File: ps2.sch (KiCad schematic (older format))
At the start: 10 parts

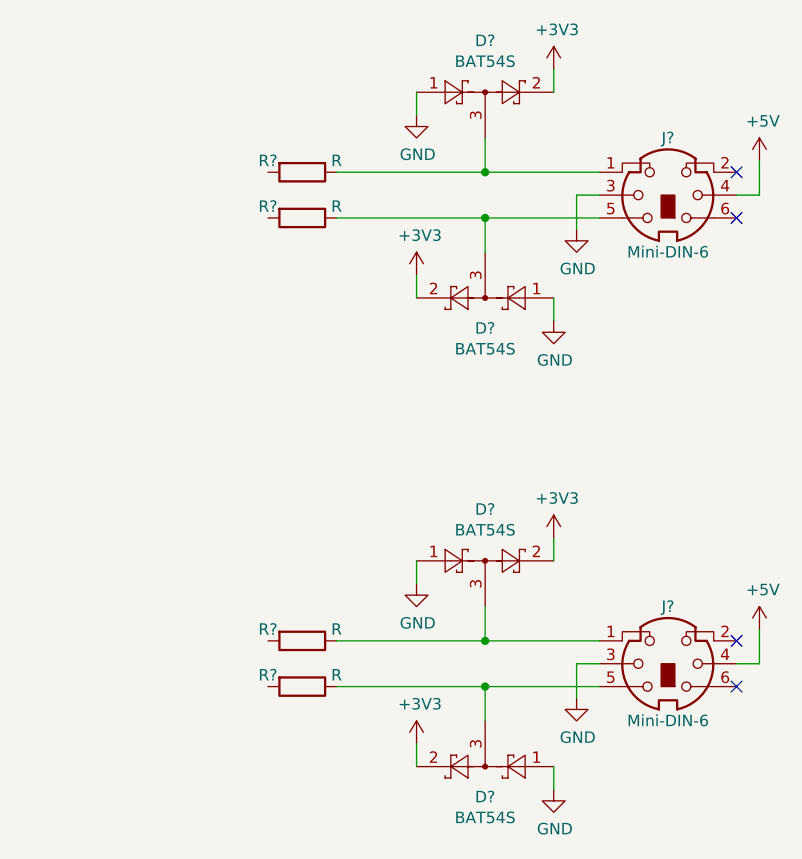
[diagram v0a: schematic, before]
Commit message: HDMI and VGA circuit added.
Signed-off-by: Kali Prasad <kprasadvnsi@protonmail.com>
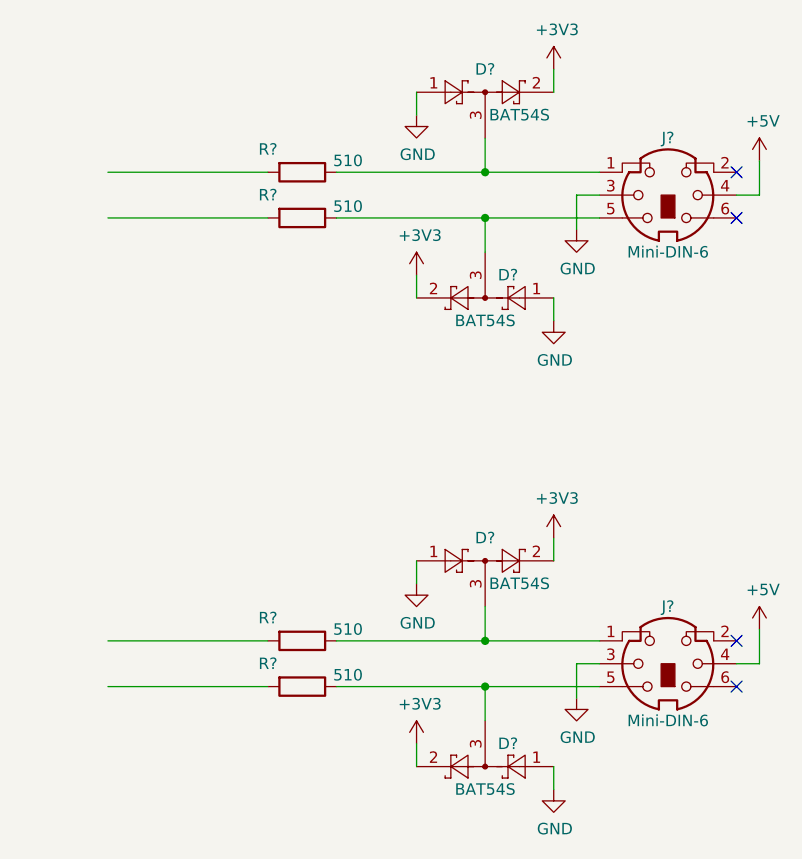
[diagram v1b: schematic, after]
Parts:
- R? (x4): value R -> 510
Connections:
- wire segments 28 -> 32
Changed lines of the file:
@@
 U 1 1 5D07F41B
 P 5150 2200
-F 0 "D?" H 5150 2425 50  0000 C CNN
-F 1 "BAT54S" H 5150 2334 50  0000 C CNN
+F 0 "D?" H 5150 2300 50  0000 C CNN
+F 1 "BAT54S" H 5300 2100 50  0000 C CNN
 F 2 "Package_TO_SOT_SMD:SOT-23" H 5225 2325 50  0001 L CNN
 F 3 "https://www.diodes.com/assets/Datasheets/ds11005.pdf" H 5030 2200 50  0001 C CNN
@@
 U 1 1 5D07FCC7
 P 5150 3100
-F 0 "D?" H 5150 3233 50  0000 C CNN
-F 1 "BAT54S" H 5150 3324 50  0000 C CNN
+F 0 "D?" H 5050 3000 50  0000 C CNN
+F 1 "BAT54S" H 5150 3200 50  0000 C CNN
 F 2 "Package_TO_SOT_SMD:SOT-23" H 5225 3225 50  0001 L CNN
 F 3 "https://www.diodes.com/assets/Datasheets/ds11005.pdf" H 5030 3100 50  0001 C CNN
@@
 U 1 1 5D080306
 P 4350 2550
-F 0 "R?" V 4300 2400 50  0000 C CNN
-F 1 "R" V 4300 2700 50  0000 C CNN
+F 0 "R?" V 4250 2400 50  0000 C CNN
+F 1 "510" V 4300 2750 50  0000 C CNN
 F 2 "" V 4280 2550 50  0001 C CNN
 F 3 "~" H 4350 2550 50  0001 C CNN
@@
 U 1 1 5D080849
 P 4350 2750
-F 0 "R?" V 4300 2600 50  0000 C CNN
-F 1 "R" V 4300 2900 50  0000 C CNN
+F 0 "R?" V 4250 2600 50  0000 C CNN
+F 1 "510" V 4300 2950 50  0000 C CNN
 F 2 "" V 4280 2750 50  0001 C CNN
 F 3 "~" H 4350 2750 50  0001 C CNN
@@
 U 1 1 5D0BA90B
 P 5150 4250
-F 0 "D?" H 5150 4475 50  0000 C CNN
-F 1 "BAT54S" H 5150 4384 50  0000 C CNN
+F 0 "D?" H 5150 4350 50  0000 C CNN
+F 1 "BAT54S" H 5300 4150 50  0000 C CNN
 F 2 "Package_TO_SOT_SMD:SOT-23" H 5225 4375 50  0001 L CNN
 F 3 "https://www.diodes.com/assets/Datasheets/ds11005.pdf" H 5030 4250 50  0001 C CNN
@@
 U 1 1 5D0BA915
 P 5150 5150
-F 0 "D?" H 5150 5283 50  0000 C CNN
-F 1 "BAT54S" H 5150 5374 50  0000 C CNN
+F 0 "D?" H 5050 5050 50  0000 C CNN
+F 1 "BAT54S" H 5150 5250 50  0000 C CNN
 F 2 "Package_TO_SOT_SMD:SOT-23" H 5225 5275 50  0001 L CNN
 F 3 "https://www.diodes.com/assets/Datasheets/ds11005.pdf" H 5030 5150 50  0001 C CNN
@@
 U 1 1 5D0BA91F
 P 4350 4600
-F 0 "R?" V 4300 4450 50  0000 C CNN
-F 1 "R" V 4300 4750 50  0000 C CNN
+F 0 "R?" V 4250 4450 50  0000 C CNN
+F 1 "510" V 4300 4800 50  0000 C CNN
 F 2 "" V 4280 4600 50  0001 C CNN
 F 3 "~" H 4350 4600 50  0001 C CNN
@@
 U 1 1 5D0BA929
 P 4350 4800
-F 0 "R?" V 4300 4650 50  0000 C CNN
-F 1 "R" V 4300 4950 50  0000 C CNN
+F 0 "R?" V 4250 4650 50  0000 C CNN
+F 1 "510" V 4300 5000 50  0000 C CNN
 F 2 "" V 4280 4800 50  0001 C CNN
 F 3 "~" H 4350 4800 50  0001 C CNN
@@
 Wire Wire Line
 	6350 4550 6350 4700
+Wire Wire Line
+	4200 2550 3500 2550
+Wire Wire Line
+	4200 2750 3500 2750
+Wire Wire Line
+	4200 4600 3500 4600
+Wire Wire Line
+	4200 4800 3500 4800
 $EndSCHEMATC

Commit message: SOM added.
Signed-off-by: Kali Prasad <kprasadvnsi@protonmail.com>
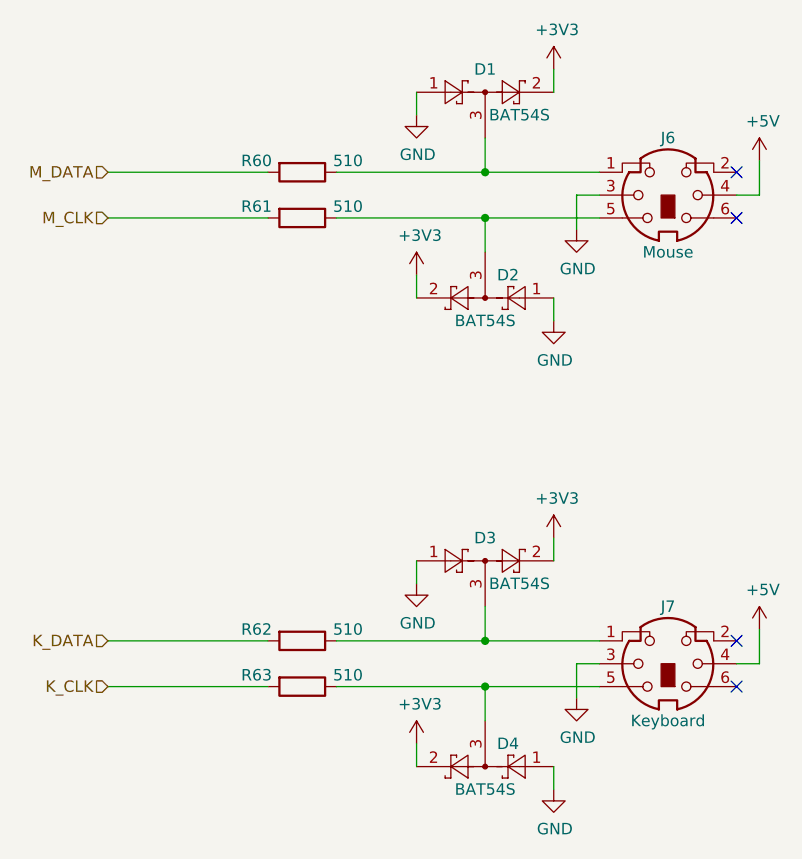
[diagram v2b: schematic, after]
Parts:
- J6: renamed from J?; value Mini-DIN-6 -> Mouse; footprint (none) -> lt_eval_board:Mini_din6
- J7: renamed from J?; value Mini-DIN-6 -> Keyboard; footprint (none) -> lt_eval_board:Mini_din6
- R60, R61, R62, R63: renamed from R?; footprint (none) -> Resistor_SMD:R_0805_2012Metric_Pad1.15x1.40mm_HandSolder
- gave numbers to parts that had none: 4
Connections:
- net labels added: K_CLK, K_DATA, M_CLK, M_DATA
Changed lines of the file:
@@
 $Descr A4 11693 8268
 encoding utf-8
-Sheet 7 7
+Sheet 4 8
 Title "LT_Eval_board"
 Date "2019-06-16"
@@
 $EndDescr
 $Comp
-L Diode:BAT54S D?
+L Diode:BAT54S D1
 U 1 1 5D07F41B
 P 5150 2200
-F 0 "D?" H 5150 2300 50  0000 C CNN
+F 0 "D1" H 5150 2300 50  0000 C CNN
 F 1 "BAT54S" H 5300 2100 50  0000 C CNN
 F 2 "Package_TO_SOT_SMD:SOT-23" H 5225 2325 50  0001 L CNN
@@
 $EndComp
 $Comp
-L Diode:BAT54S D?
+L Diode:BAT54S D2
 U 1 1 5D07FCC7
 P 5150 3100
-F 0 "D?" H 5050 3000 50  0000 C CNN
+F 0 "D2" H 5050 3000 50  0000 C CNN
 F 1 "BAT54S" H 5150 3200 50  0000 C CNN
 F 2 "Package_TO_SOT_SMD:SOT-23" H 5225 3225 50  0001 L CNN
@@
 $EndComp
 $Comp
-L Device:R R?
+L Device:R R60
 U 1 1 5D080306
 P 4350 2550
-F 0 "R?" V 4250 2400 50  0000 C CNN
+F 0 "R60" V 4300 2350 50  0000 C CNN
 F 1 "510" V 4300 2750 50  0000 C CNN
-F 2 "" V 4280 2550 50  0001 C CNN
+F 2 "Resistor_SMD:R_0805_2012Metric_Pad1.15x1.40mm_HandSolder" V 4280 2550 50  0001 C CNN
 F 3 "~" H 4350 2550 50  0001 C CNN
 	1    4350 2550
@@
 $EndComp
 $Comp
-L Device:R R?
+L Device:R R61
 U 1 1 5D080849
 P 4350 2750
-F 0 "R?" V 4250 2600 50  0000 C CNN
+F 0 "R61" V 4300 2550 50  0000 C CNN
 F 1 "510" V 4300 2950 50  0000 C CNN
-F 2 "" V 4280 2750 50  0001 C CNN
+F 2 "Resistor_SMD:R_0805_2012Metric_Pad1.15x1.40mm_HandSolder" V 4280 2750 50  0001 C CNN
 F 3 "~" H 4350 2750 50  0001 C CNN
 	1    4350 2750
@@
 $EndComp
 $Comp
-L Connector:Mini-DIN-6 J?
+L Connector:Mini-DIN-6 J6
 U 1 1 5D07D04B
 P 5950 2650
-F 0 "J?" H 5950 2400 50  0000 C CNN
-F 1 "Mini-DIN-6" H 5950 2900 50  0000 C CNN
-F 2 "" H 5950 2650 50  0001 C CNN
+F 0 "J6" H 5950 2400 50  0000 C CNN
+F 1 "Mouse" H 5950 2900 50  0000 C CNN
+F 2 "lt_eval_board:Mini_din6" H 5950 2650 50  0001 C CNN
 F 3 "http://service.powerdynamics.com/ec/Catalog17/Section%2011.pdf" H 5950 2650 50  0001 C CNN
 	1    5950 2650
@@
 	5150 2550 5650 2550
 $Comp
-L power:GND #PWR?
+L power:GND #PWR028
 U 1 1 5D094AF6
 P 4850 2300
-F 0 "#PWR?" H 4850 2050 50  0001 C CNN
+F 0 "#PWR028" H 4850 2050 50  0001 C CNN
 F 1 "GND" H 4855 2127 50  0000 C CNN
 F 2 "" H 4850 2300 50  0001 C CNN
@@
 	5150 2400 5150 2550
 $Comp
-L power:+3V3 #PWR?
+L power:+3V3 #PWR032
 U 1 1 5D095BB7
 P 5450 2100
-F 0 "#PWR?" H 5450 1950 50  0001 C CNN
+F 0 "#PWR032" H 5450 1950 50  0001 C CNN
 F 1 "+3V3" H 5465 2273 50  0000 C CNN
 F 2 "" H 5450 2100 50  0001 C CNN
@@
 	5150 2750 5650 2750
 $Comp
-L power:+3V3 #PWR?
+L power:+3V3 #PWR029
 U 1 1 5D09F81C
 P 4850 3000
-F 0 "#PWR?" H 4850 2850 50  0001 C CNN
+F 0 "#PWR029" H 4850 2850 50  0001 C CNN
 F 1 "+3V3" H 4865 3173 50  0000 C CNN
 F 2 "" H 4850 3000 50  0001 C CNN
@@
 $EndComp
 $Comp
-L power:GND #PWR?
+L power:GND #PWR033
 U 1 1 5D0A0712
 P 5450 3200
-F 0 "#PWR?" H 5450 2950 50  0001 C CNN
+F 0 "#PWR033" H 5450 2950 50  0001 C CNN
 F 1 "GND" H 5455 3027 50  0000 C CNN
 F 2 "" H 5450 3200 50  0001 C CNN
@@
 NoConn ~ 6250 2750
 $Comp
-L power:GND #PWR?
+L power:GND #PWR036
 U 1 1 5D0A2D26
 P 5550 2800
-F 0 "#PWR?" H 5550 2550 50  0001 C CNN
+F 0 "#PWR036" H 5550 2550 50  0001 C CNN
 F 1 "GND" H 5555 2627 50  0000 C CNN
 F 2 "" H 5550 2800 50  0001 C CNN
@@
 	5650 2650 5550 2650
 $Comp
-L power:+5V #PWR?
+L power:+5V #PWR038
 U 1 1 5D0A37AF
 P 6350 2500
-F 0 "#PWR?" H 6350 2350 50  0001 C CNN
+F 0 "#PWR038" H 6350 2350 50  0001 C CNN
 F 1 "+5V" H 6365 2673 50  0000 C CNN
 F 2 "" H 6350 2500 50  0001 C CNN
@@
 	6350 2500 6350 2650
 $Comp
-L Diode:BAT54S D?
+L Diode:BAT54S D3
 U 1 1 5D0BA90B
 P 5150 4250
-F 0 "D?" H 5150 4350 50  0000 C CNN
+F 0 "D3" H 5150 4350 50  0000 C CNN
 F 1 "BAT54S" H 5300 4150 50  0000 C CNN
 F 2 "Package_TO_SOT_SMD:SOT-23" H 5225 4375 50  0001 L CNN
@@
 $EndComp
 $Comp
-L Diode:BAT54S D?
+L Diode:BAT54S D4
 U 1 1 5D0BA915
 P 5150 5150
-F 0 "D?" H 5050 5050 50  0000 C CNN
+F 0 "D4" H 5050 5050 50  0000 C CNN
 F 1 "BAT54S" H 5150 5250 50  0000 C CNN
 F 2 "Package_TO_SOT_SMD:SOT-23" H 5225 5275 50  0001 L CNN
@@
 $EndComp
 $Comp
-L Device:R R?
+L Device:R R62
 U 1 1 5D0BA91F
 P 4350 4600
-F 0 "R?" V 4250 4450 50  0000 C CNN
+F 0 "R62" V 4300 4400 50  0000 C CNN
 F 1 "510" V 4300 4800 50  0000 C CNN
-F 2 "" V 4280 4600 50  0001 C CNN
+F 2 "Resistor_SMD:R_0805_2012Metric_Pad1.15x1.40mm_HandSolder" V 4280 4600 50  0001 C CNN
 F 3 "~" H 4350 4600 50  0001 C CNN
 	1    4350 4600
@@
 $EndComp
 $Comp
-L Device:R R?
+L Device:R R63
 U 1 1 5D0BA929
 P 4350 4800
-F 0 "R?" V 4250 4650 50  0000 C CNN
+F 0 "R63" V 4300 4600 50  0000 C CNN
 F 1 "510" V 4300 5000 50  0000 C CNN
-F 2 "" V 4280 4800 50  0001 C CNN
+F 2 "Resistor_SMD:R_0805_2012Metric_Pad1.15x1.40mm_HandSolder" V 4280 4800 50  0001 C CNN
 F 3 "~" H 4350 4800 50  0001 C CNN
 	1    4350 4800
@@
 $EndComp
 $Comp
-L Connector:Mini-DIN-6 J?
+L Connector:Mini-DIN-6 J7
 U 1 1 5D0BA933
 P 5950 4700
-F 0 "J?" H 5950 4450 50  0000 C CNN
-F 1 "Mini-DIN-6" H 5950 4950 50  0000 C CNN
-F 2 "" H 5950 4700 50  0001 C CNN
+F 0 "J7" H 5950 4450 50  0000 C CNN
+F 1 "Keyboard" H 5950 4950 50  0000 C CNN
+F 2 "lt_eval_board:Mini_din6" H 5950 4700 50  0001 C CNN
 F 3 "http://service.powerdynamics.com/ec/Catalog17/Section%2011.pdf" H 5950 4700 50  0001 C CNN
 	1    5950 4700
@@
 	5150 4600 5650 4600
 $Comp
-L power:GND #PWR?
+L power:GND #PWR030
 U 1 1 5D0BA940
 P 4850 4350
-F 0 "#PWR?" H 4850 4100 50  0001 C CNN
+F 0 "#PWR030" H 4850 4100 50  0001 C CNN
 F 1 "GND" H 4855 4177 50  0000 C CNN
 F 2 "" H 4850 4350 50  0001 C CNN
@@
 	5150 4450 5150 4600
 $Comp
-L power:+3V3 #PWR?
+L power:+3V3 #PWR034
 U 1 1 5D0BA94C
 P 5450 4150
-F 0 "#PWR?" H 5450 4000 50  0001 C CNN
+F 0 "#PWR034" H 5450 4000 50  0001 C CNN
 F 1 "+3V3" H 5465 4323 50  0000 C CNN
 F 2 "" H 5450 4150 50  0001 C CNN
@@
 	5150 4800 5650 4800
 $Comp
-L power:+3V3 #PWR?
+L power:+3V3 #PWR031
 U 1 1 5D0BA95B
 P 4850 5050
-F 0 "#PWR?" H 4850 4900 50  0001 C CNN
+F 0 "#PWR031" H 4850 4900 50  0001 C CNN
 F 1 "+3V3" H 4865 5223 50  0000 C CNN
 F 2 "" H 4850 5050 50  0001 C CNN
@@
 $EndComp
 $Comp
-L power:GND #PWR?
+L power:GND #PWR035
 U 1 1 5D0BA965
 P 5450 5250
-F 0 "#PWR?" H 5450 5000 50  0001 C CNN
+F 0 "#PWR035" H 5450 5000 50  0001 C CNN
 F 1 "GND" H 5455 5077 50  0000 C CNN
 F 2 "" H 5450 5250 50  0001 C CNN
@@
 NoConn ~ 6250 4800
 $Comp
-L power:GND #PWR?
+L power:GND #PWR037
 U 1 1 5D0BA973
 P 5550 4850
-F 0 "#PWR?" H 5550 4600 50  0001 C CNN
+F 0 "#PWR037" H 5550 4600 50  0001 C CNN
 F 1 "GND" H 5555 4677 50  0000 C CNN
 F 2 "" H 5550 4850 50  0001 C CNN
@@
 	5650 4700 5550 4700
 $Comp
-L power:+5V #PWR?
+L power:+5V #PWR039
 U 1 1 5D0BA97E
 P 6350 4550
-F 0 "#PWR?" H 6350 4400 50  0001 C CNN
+F 0 "#PWR039" H 6350 4400 50  0001 C CNN
 F 1 "+5V" H 6365 4723 50  0000 C CNN
 F 2 "" H 6350 4550 50  0001 C CNN
@@
 Wire Wire Line
 	4200 4800 3500 4800
+Text HLabel 3500 2550 0    50   Input ~ 0
+M_DATA
+Text HLabel 3500 2750 0    50   Input ~ 0
+M_CLK
+Text HLabel 3500 4600 0    50   Input ~ 0
+K_DATA
+Text HLabel 3500 4800 0    50   Input ~ 0
+K_CLK
 $EndSCHEMATC
